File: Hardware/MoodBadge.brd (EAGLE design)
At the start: 195.6 x 195.6 mm, 80 parts, among them IC1 PCF8574T, U2 ATMEGA328P_TQFP, Y1 Crystal-CA-310

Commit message: Initial placement of components
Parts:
- moved LIPO 269.8 mm to (50.8, 6.35), turned to 270 degrees
- moved LED8 268.0 mm to (38.1, 17.8), turned to 270 degrees
- moved R24 265.4 mm to (34.3, 17.8), turned to 270 degrees
- moved C1 264.0 mm to (41.9, -15.2), turned to 270 degrees
- moved R16 261.0 mm to (24.1, 17.8)
- moved R17 261.0 mm to (24.1, 12.7)
- moved R18 261.0 mm to (24.1, 7.62)
- moved R19 261.0 mm to (24.1, 2.54)
- moved R20 261.0 mm to (24.1, -2.54)
- moved R21 261.0 mm to (24.1, -7.62)
- moved R22 261.0 mm to (24.1, -12.7)
- moved R23 261.0 mm to (24.1, -17.8)
- moved ON/OFF 256.6 mm to (45.7, 16.5), turned to 180 degrees
- moved IC1 243.8 mm to (19.1, 27.9), turned to 90 degrees
- moved OP 221.8 mm to (-21.6, 20.3), turned to 90 degrees
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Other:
- board size 195.6 x 195.6 mm -> 114.3 x 114.3 mm

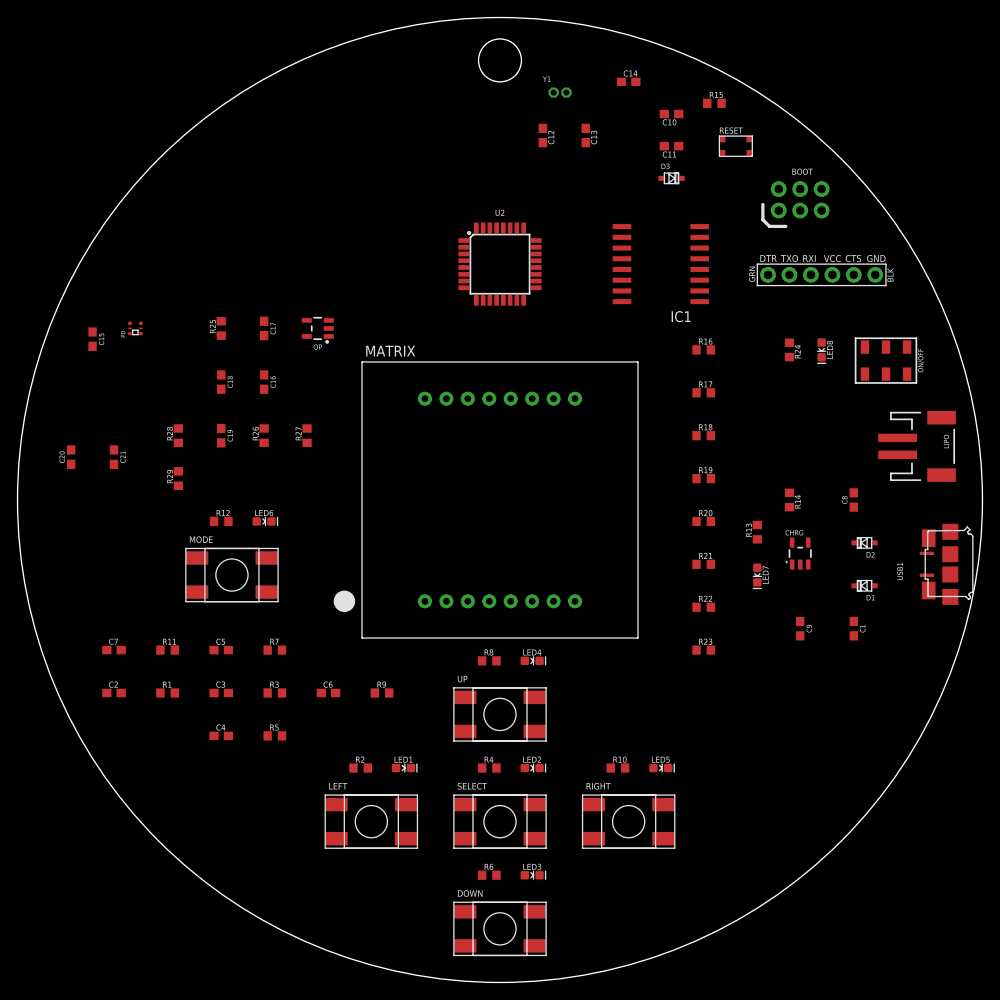
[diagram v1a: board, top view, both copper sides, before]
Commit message: Continued routing and changed a few pins for easier routing
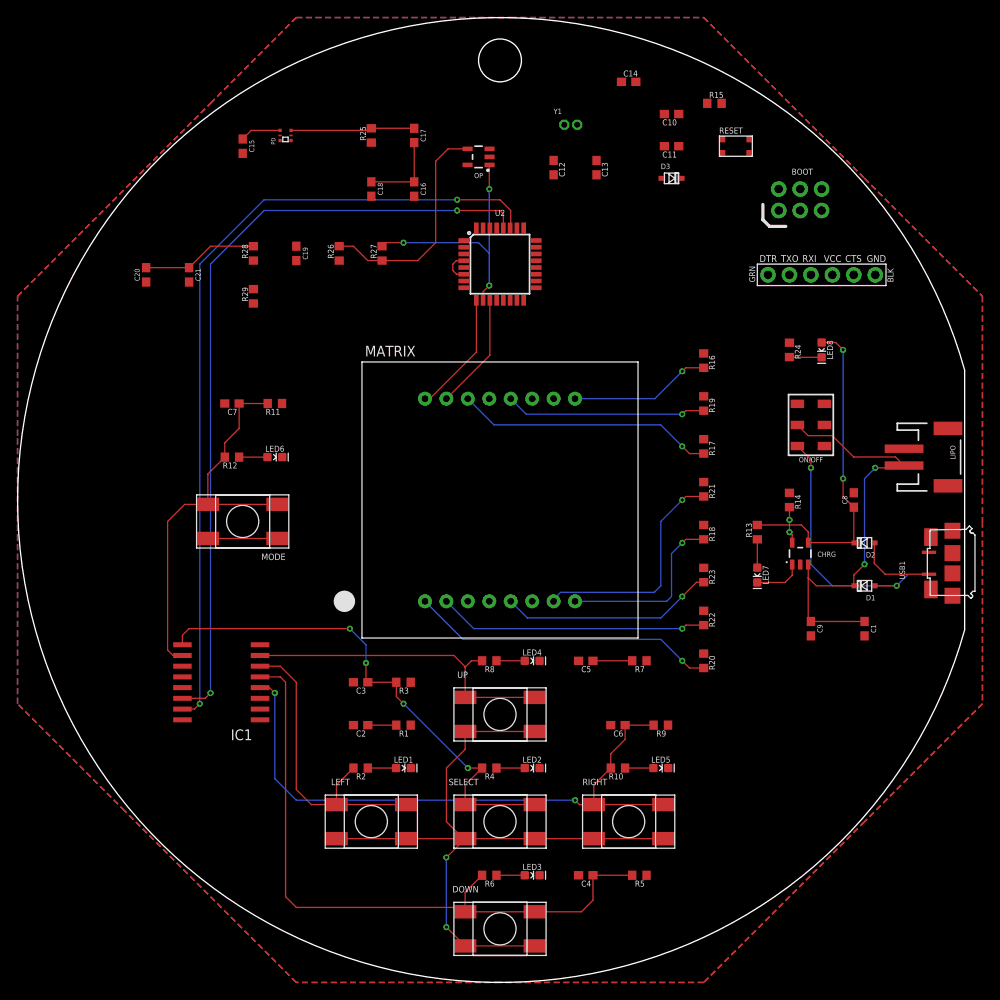
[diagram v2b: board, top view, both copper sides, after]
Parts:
- moved IC1 71.9 mm to (-33.0, -21.6)
- moved C4 46.2 mm to (10.2, -44.5), turned to 180 degrees
- moved R5 46.2 mm to (16.5, -44.5), turned to 180 degrees
- moved C5 43.2 mm to (10.2, -19.1), turned to 180 degrees
- moved R7 43.2 mm to (16.5, -19.1), turned to 180 degrees
- moved C6 34.5 mm to (14.0, -26.7), turned to 180 degrees
- moved R9 33.2 mm to (19.1, -26.7), turned to 180 degrees
- moved C7 32.4 mm to (-31.8, 11.4), turned to 180 degrees
- moved R11 31.9 mm to (-26.7, 11.4), turned to 180 degrees
- moved C2 29.5 mm to (-16.5, -26.7), turned to 180 degrees
- moved C16 29.0 mm to (-10.2, 36.8)
- moved C17 29.0 mm to (-10.2, 43.2)
- moved C18 29.0 mm to (-15.2, 36.8)
- moved PD 29.0 mm to (-25.4, 43.2)
- moved R25 29.0 mm to (-15.2, 43.2)
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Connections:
- net RIGHT: now also IC1.4; no longer IC1.7
- net UP: now also IC1.7; no longer IC1.4
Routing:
- net VCC: track 0.00 -> 154.8 mm, vias 0 -> 4
- net SDA: track 0.00 -> 97.0 mm, vias 0 -> 2
- net SCL: track 0.00 -> 93.5 mm, vias 0 -> 2
- net DOWN: track 0.00 -> 79.2 mm
- net RIGHT: track 0.00 -> 73.8 mm, vias 0 -> 2
- net SELECT: track 0.00 -> 60.7 mm, vias 0 -> 4
- net VLIPO: track 0.00 -> 52.4 mm, vias 0 -> 2
- net MODE: track 0.00 -> 48.0 mm
- net UP: track 0.00 -> 43.7 mm
- net LEFT: track 0.00 -> 40.1 mm
- net N$18: track 0.00 -> 36.3 mm, vias 0 -> 1
- net N$20: track 0.00 -> 32.0 mm, vias 0 -> 1
- net N$15: track 0.00 -> 30.6 mm, vias 0 -> 1
- net N$2: track 0.00 -> 30.3 mm, vias 0 -> 2
- net PULSE: track 0.00 -> 29.8 mm, vias 0 -> 3
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- added copper zone on layer 1, net GND
- added copper zone on layer 16, net GND
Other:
- board size 114.3 x 114.3 mm -> 112.2 x 114.3 mm

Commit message: Edited copper pour outline for easier visibility
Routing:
- net VCC: track 154.8 -> 210.6 mm, vias 4 -> 6
- net N$25: track 0.00 -> 42.7 mm, vias 0 -> 2
- net N$26: track 0.00 -> 19.6 mm
- net LD10: track 0.00 -> 13.1 mm
- net LD11: track 0.00 -> 12.4 mm
- net LD13: track 0.00 -> 12.3 mm
- net N$28: track 27.0 -> 27.8 mm
- removed copper zone on layer 1, net GND
- removed copper zone on layer 16, net GND
